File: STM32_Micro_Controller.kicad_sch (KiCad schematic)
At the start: 1 part, among them U1 STM32F103C8T6

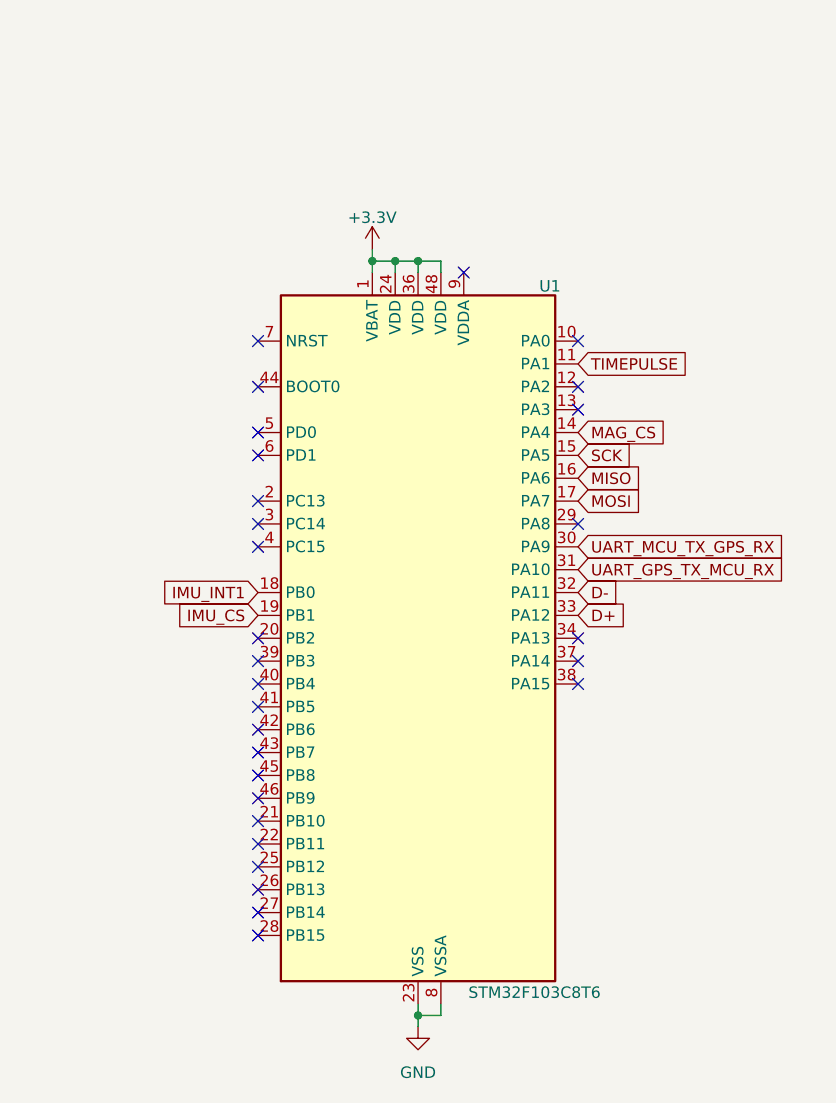
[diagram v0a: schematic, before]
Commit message: Changed the wording of the labels to fit SPI
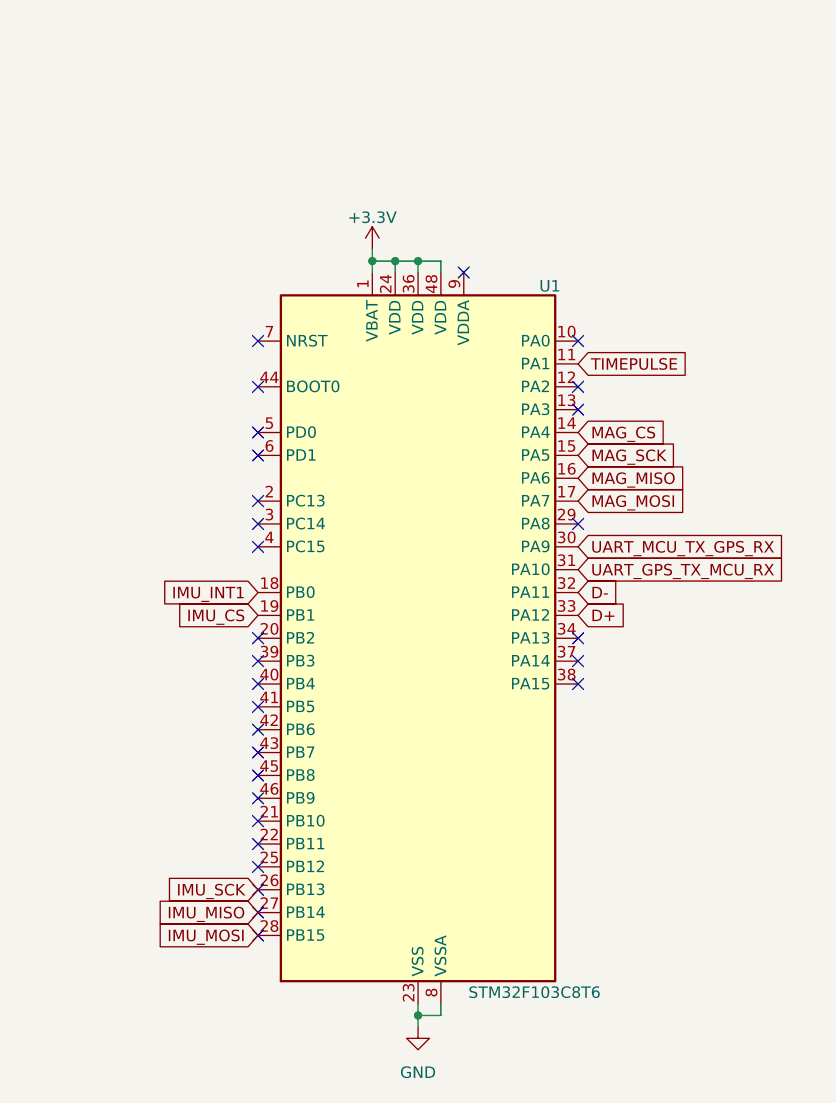
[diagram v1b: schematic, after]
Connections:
- net IMU_SCK: now reaches U1.26 (PB13)
- net IMU_MISO: now reaches U1.27 (PB14)
- net IMU_MOSI: now reaches U1.28 (PB15)
- net MISO renamed MAG_MISO
- net MOSI renamed MAG_MOSI
- net SCK renamed MAG_SCK
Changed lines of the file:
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@@
 		)
 	)
-	(global_label "SCK"
+	(global_label "MAG_SCK"
 		(shape input)
 		(at 148.59 72.39 0)
@@
 		)
 		(property "Intersheetrefs" "${INTERSHEET_REFS}"
-			(at 155.3247 72.39 0)
+			(at 160.1023 72.39 0)
 			(effects
 				(font
@@
 		)
 	)
+	(global_label "IMU_MISO"
+		(shape input)
+		(at 113.03 123.19 180)
+		(fields_autoplaced yes)
+		(effects
+			(font
+				(size 1.27 1.27)
+			)
+			(justify right)
+		)
+		(property "Intersheetrefs" "${INTERSHEET_REFS}"
+			(at 101.0943 123.19 0)
+			(effects
+				(font
+					(size 1.27 1.27)
+				)
+				(justify right)
+				(hide yes)
+			)
+		)
+	)
 	(global_label "IMU_INT1"
 		(shape input)
@@
 		)
 	)
-	(global_label "MISO"
+	(global_label "MAG_MISO"
 		(shape input)
 		(at 148.59 74.93 0)
@@
 		)
 		(property "Intersheetrefs" "${INTERSHEET_REFS}"
-			(at 156.1714 74.93 0)
+			(at 160.949 74.93 0)
 			(effects
 				(font
@@
 		)
 	)
+	(global_label "IMU_MOSI"
+		(shape input)
+		(at 113.03 125.73 180)
+		(fields_autoplaced yes)
+		(effects
+			(font
+				(size 1.27 1.27)
+			)
+			(justify right)
+		)
+		(property "Intersheetrefs" "${INTERSHEET_REFS}"
+			(at 101.0943 125.73 0)
+			(effects
+				(font
+					(size 1.27 1.27)
+				)
+				(justify right)
+				(hide yes)
+			)
+		)
+	)
 	(global_label "D+"
 		(shape input)
@@
 		)
 	)
-	(global_label "MOSI"
+	(global_label "IMU_SCK"
+		(shape input)
+		(at 113.03 120.65 180)
+		(fields_autoplaced yes)
+		(effects
+			(font
+				(size 1.27 1.27)
+			)
+			(justify right)
+		)
+		(property "Intersheetrefs" "${INTERSHEET_REFS}"
+			(at 101.941 120.65 0)
+			(effects
+				(font
+					(size 1.27 1.27)
+				)
+				(justify right)
+				(hide yes)
+			)
+		)
+	)
+	(global_label "MAG_MOSI"
 		(shape input)
 		(at 148.59 77.47 0)
@@
 		)
 		(property "Intersheetrefs" "${INTERSHEET_REFS}"
-			(at 156.1714 77.47 0)
-			(effects
-				(font
+			(at 160.949 77.47 0)
+			(effects
+				(font

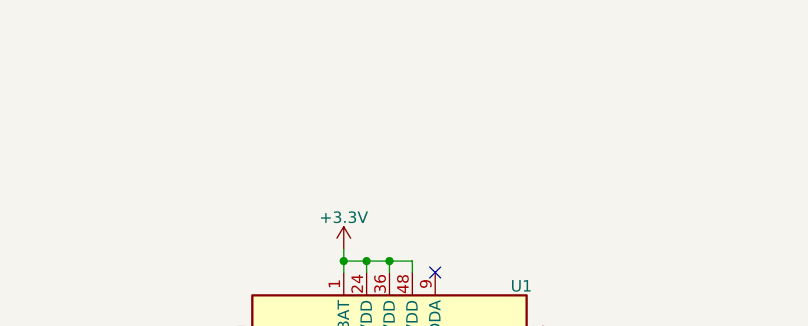
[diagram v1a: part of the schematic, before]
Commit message: Added the Sheet for the SD card and started the schematic.
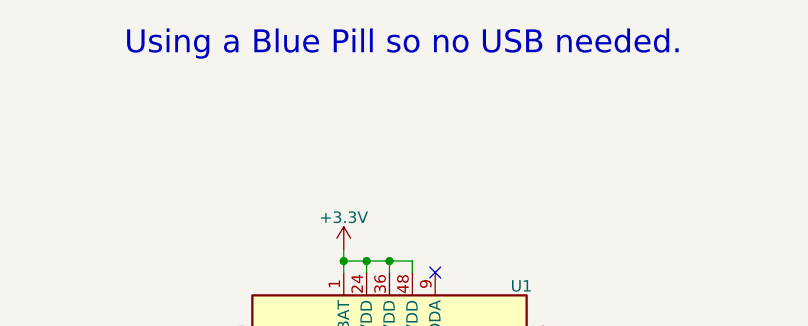
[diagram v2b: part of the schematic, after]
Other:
- note added: "Using a Blue Pill so no USB needed."
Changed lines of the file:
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@@
 	(generator_version "9.0")
 	(paper "A4")
+	(text "Using a Blue Pill so no USB needed."
+		(exclude_from_sim no)
+		(at 132.334 26.67 0)
+		(effects
+			(font
+				(size 2.54 2.54)
+			)
+		)
+	)
 	(junction
 		(at 128.27 50.8)

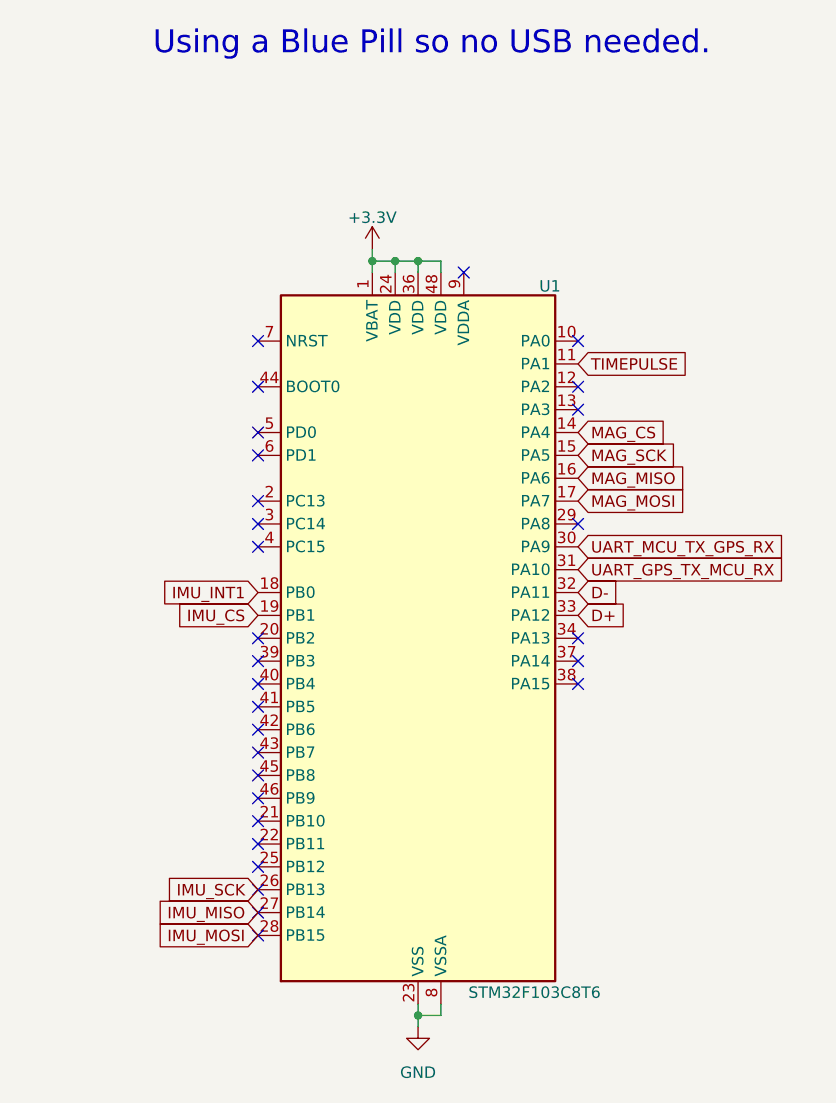
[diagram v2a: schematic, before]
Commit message: Finished the schematic for the SD.
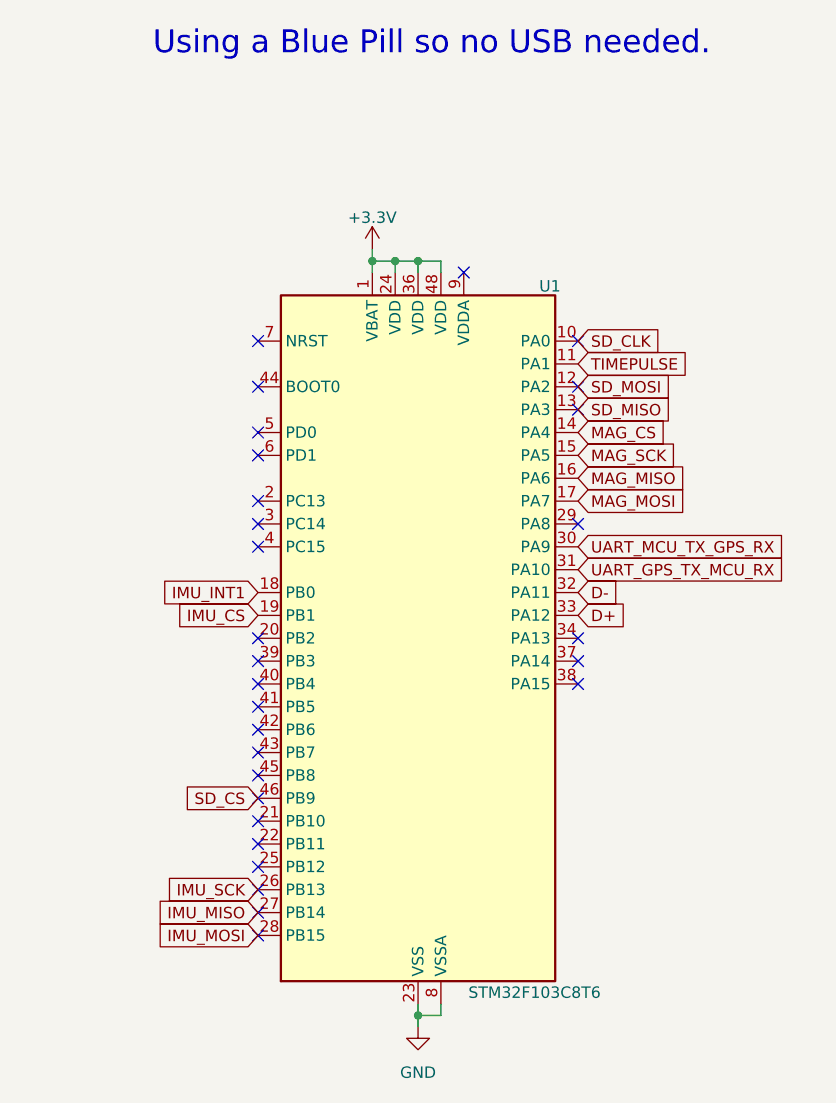
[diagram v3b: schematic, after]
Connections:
- net SD_CLK: now reaches U1.10 (PA0)
- net SD_MOSI: now reaches U1.12 (PA2)
- net SD_MISO: now reaches U1.13 (PA3)
- net SD_CS: now reaches U1.46 (PB9)
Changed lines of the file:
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@@
+		)
+	)
+	(global_label "SD_CS"
+		(shape input)
+		(at 113.03 110.49 180)
+		(fields_autoplaced yes)
+		(effects
+			(font
+				(size 1.27 1.27)
+			)
+			(justify right)
+		)
+		(property "Intersheetrefs" "${INTERSHEET_REFS}"
+			(at 104.1182 110.49 0)
+			(effects
+				(font
+					(size 1.27 1.27)
+				)
+				(justify right)
+				(hide yes)
+			)
 		)
 	)
@@
 		)
 	)
+	(global_label "SD_CLK"
+		(shape input)
+		(at 148.59 59.69 0)
+		(fields_autoplaced yes)
+		(effects
+			(font
+				(size 1.27 1.27)
+			)
+			(justify left)
+		)
+		(property "Intersheetrefs" "${INTERSHEET_REFS}"
+			(at 158.5904 59.69 0)
+			(effects
+				(font
+					(size 1.27 1.27)
+				)
+				(justify left)
+				(hide yes)
+			)
+		)
+	)
 	(global_label "IMU_MOSI"
 		(shape input)
@@
 				(hide yes)
 			)
+		)
+	)
+	(global_label "SD_MISO"
+		(shape input)
+		(at 148.59 67.31 0)
+		(fields_autoplaced yes)
+		(effects
+			(font
+				(size 1.27 1.27)
+			)
+			(justify left)
+		)
+		(property "Intersheetrefs" "${INTERSHEET_REFS}"
+			(at 159.6185 67.31 0)
+			(effects
+				(font
+					(size 1.27 1.27)
+				)
+				(justify left)
+				(hide yes)
+			)
+		)
+	)
+	(global_label "SD_MOSI"
+		(shape input)
+		(at 148.59 64.77 0)
+		(fields_autoplaced yes)
+		(effects
+			(font
+				(size 1.27 1.27)
+			)
+			(justify left)
+		)
+		(property "Intersheetrefs" "${INTERSHEET_REFS}"
+			(at 159.6185 64.77 0)
+			(effects
+				(font
+					(size 1.27 1.27)
+				)
+				(justify left)
+				(hide yes)
+			)
